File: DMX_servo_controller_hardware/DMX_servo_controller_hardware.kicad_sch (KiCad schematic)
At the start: 6 parts

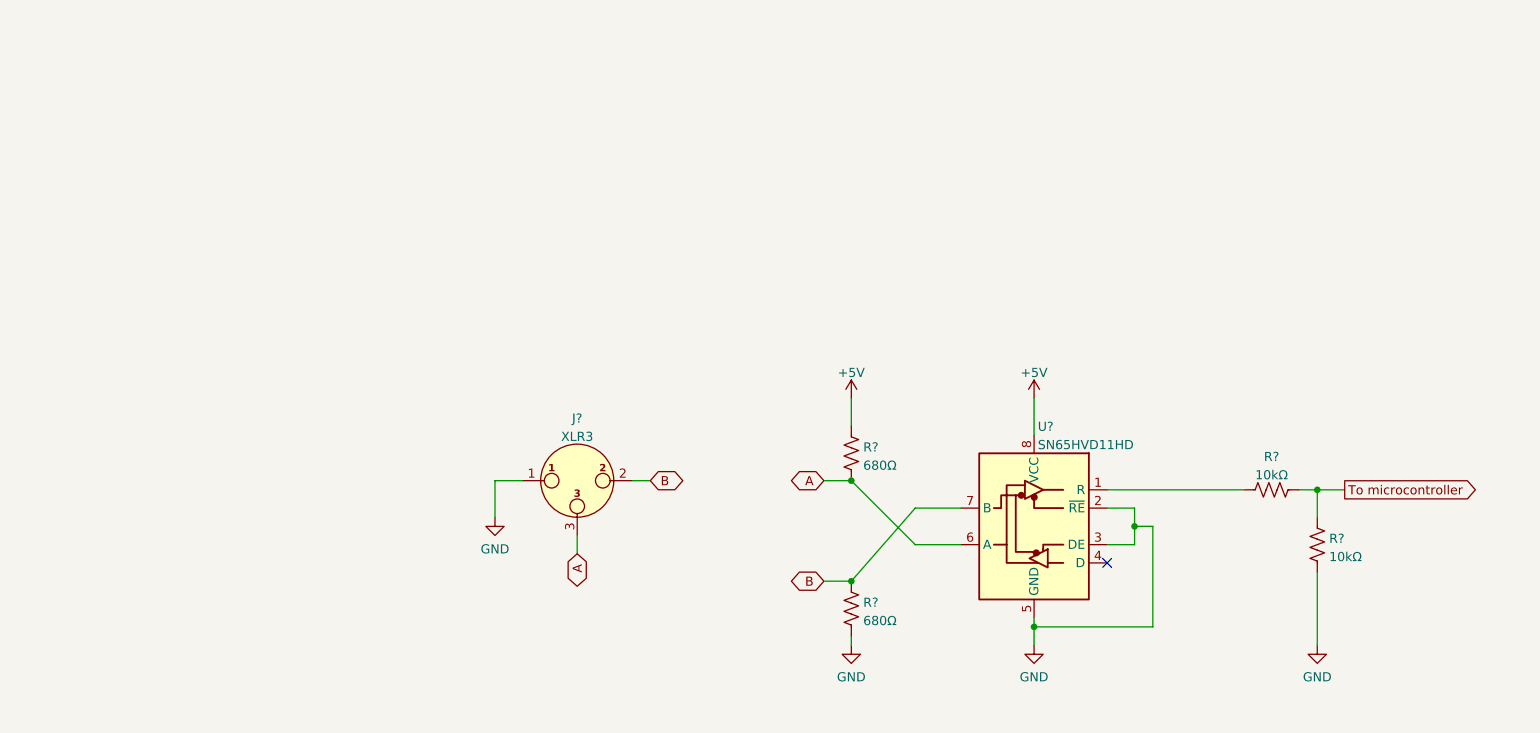
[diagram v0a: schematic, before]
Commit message: Isolates DMX signal from the rest of the electronics
We're using a 0505 5v DC/DC isolator for power and an 6N137 optocoupler
for the signal.

The 6N137 is supposed to work with 5V, but our tests (and other designs)
showed that 3.3V works fine and means the optocoupler works as a level
shifter.
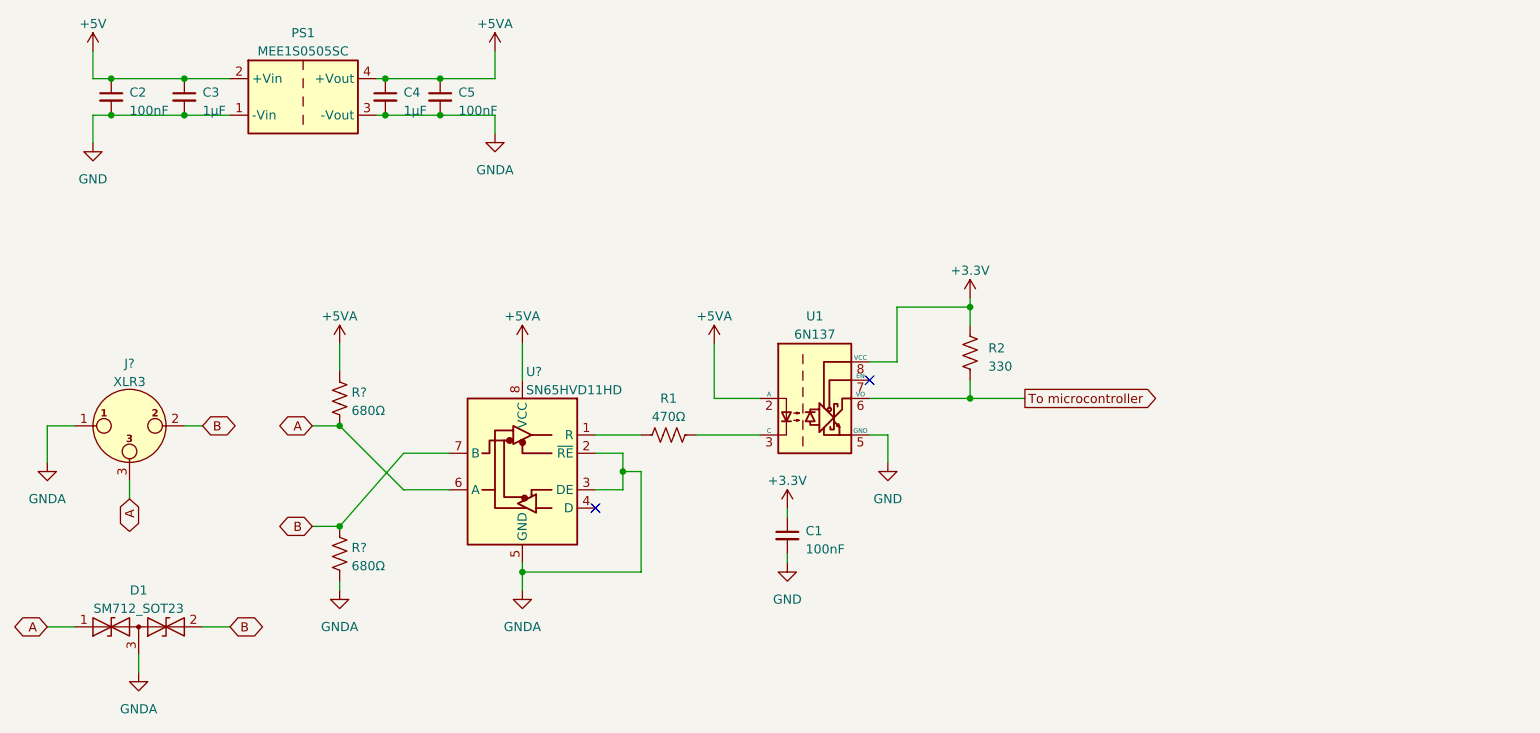
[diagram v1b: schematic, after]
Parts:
- removed R? (x2): 10kΩ, symbol Device:R_US
- added C1, C2, C5: 100nF, symbol Device:C_Small
- added C3, C4: 1μF, symbol Device:C_Small
- added D1: SM712_SOT23, Package_TO_SOT_SMD:SOT-23, symbol Diode:SM712_SOT23
- added PS1: MEE1S0505SC, Converter_DCDC:Converter_DCDC_Murata_MEE1SxxxxSC_THT, symbol Converter_DCDC:MEE1S0505SC
- added R1: 470Ω, symbol Device:R_US
- added R2: 330, symbol Device:R_US
- added U1: 6N137, Package_DIP:DIP-8_W7.62mm, symbol Isolator:6N137
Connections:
- net +5V: now also C2.1, C3.1, PS1.2 (+Vin); no longer R?.1, U?.8 (VCC)
- net A: now also D1.1 (A1)
- net B: now also D1.2 (A2)
- net GND: now also C1.2, C2.2, C3.2, PS1.1 (-Vin), U1.5 (GND); no longer J?.1, R?.2, U?.2 (~{RE}), U?.3 (DE), U?.5 (GND)
- net To microcontroller: now also R2.2, U1.6 (VO)
- net at U?.1 (R): now also R1.2
- new net: R1.1, U1.3 (C)
- new net +3.3V: C1.1, R2.1, U1.8 (VCC)
- new net +5VA: C4.1, C5.1, PS1.4 (+Vout), R?.1, U1.2 (A), U?.8 (VCC)
- new net GNDA: C4.2, C5.2, D1.3 (common), J?.1, PS1.3 (-Vout), R?.2, U?.2 (~{RE}), U?.3 (DE), U?.5 (GND)
- no-connect marks 1 -> 2
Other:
- moved on the sheet: J?, R?, U?

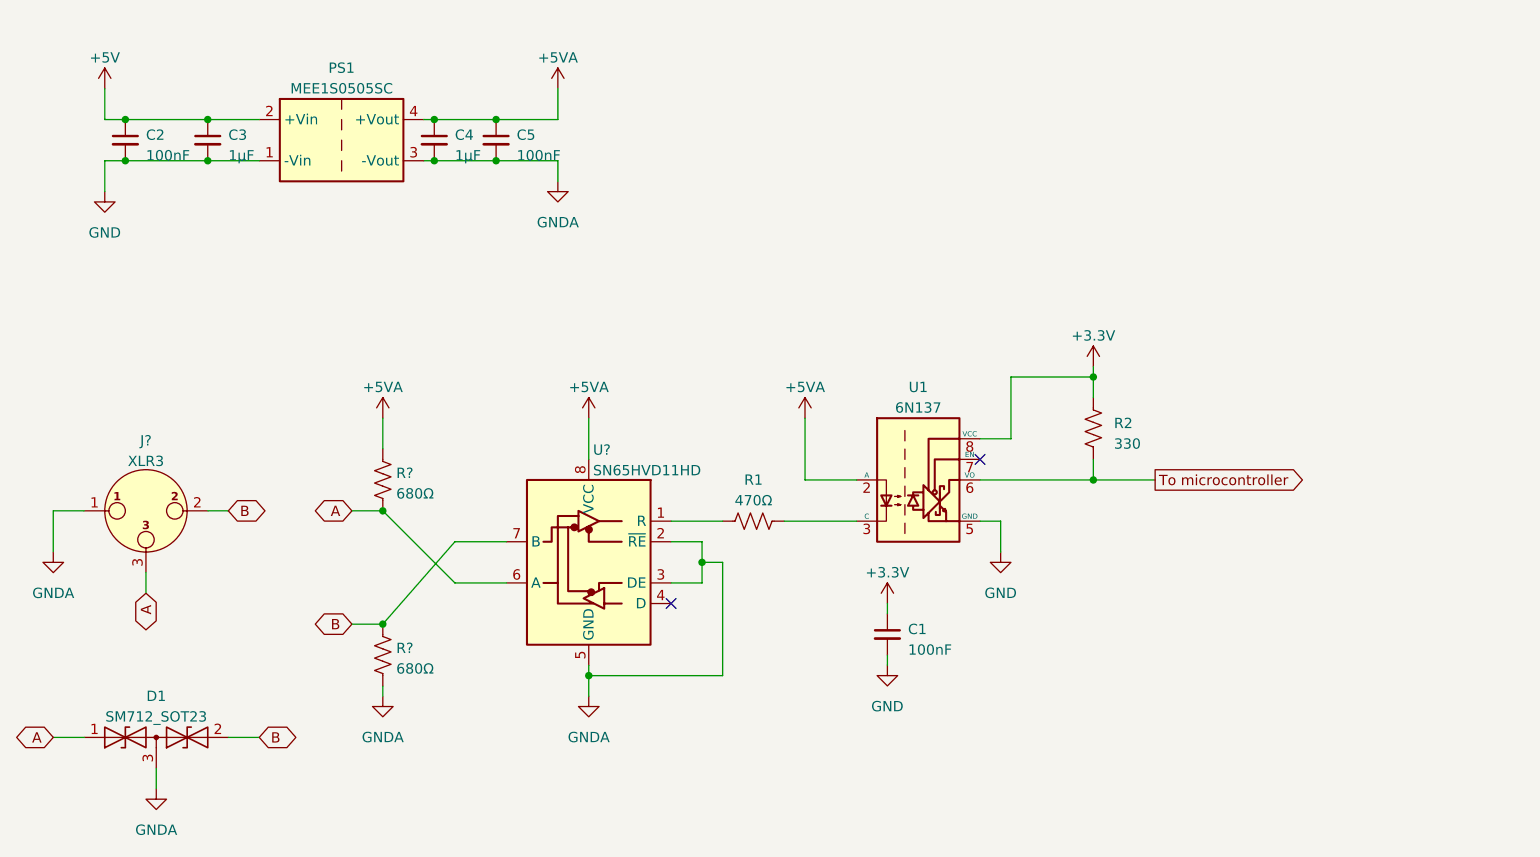
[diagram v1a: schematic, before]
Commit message: Moves XLR connector to a hierarchical sheet
The XLR connectors will be in a daughter board that can be used as a
breakout board for XLR connectors.
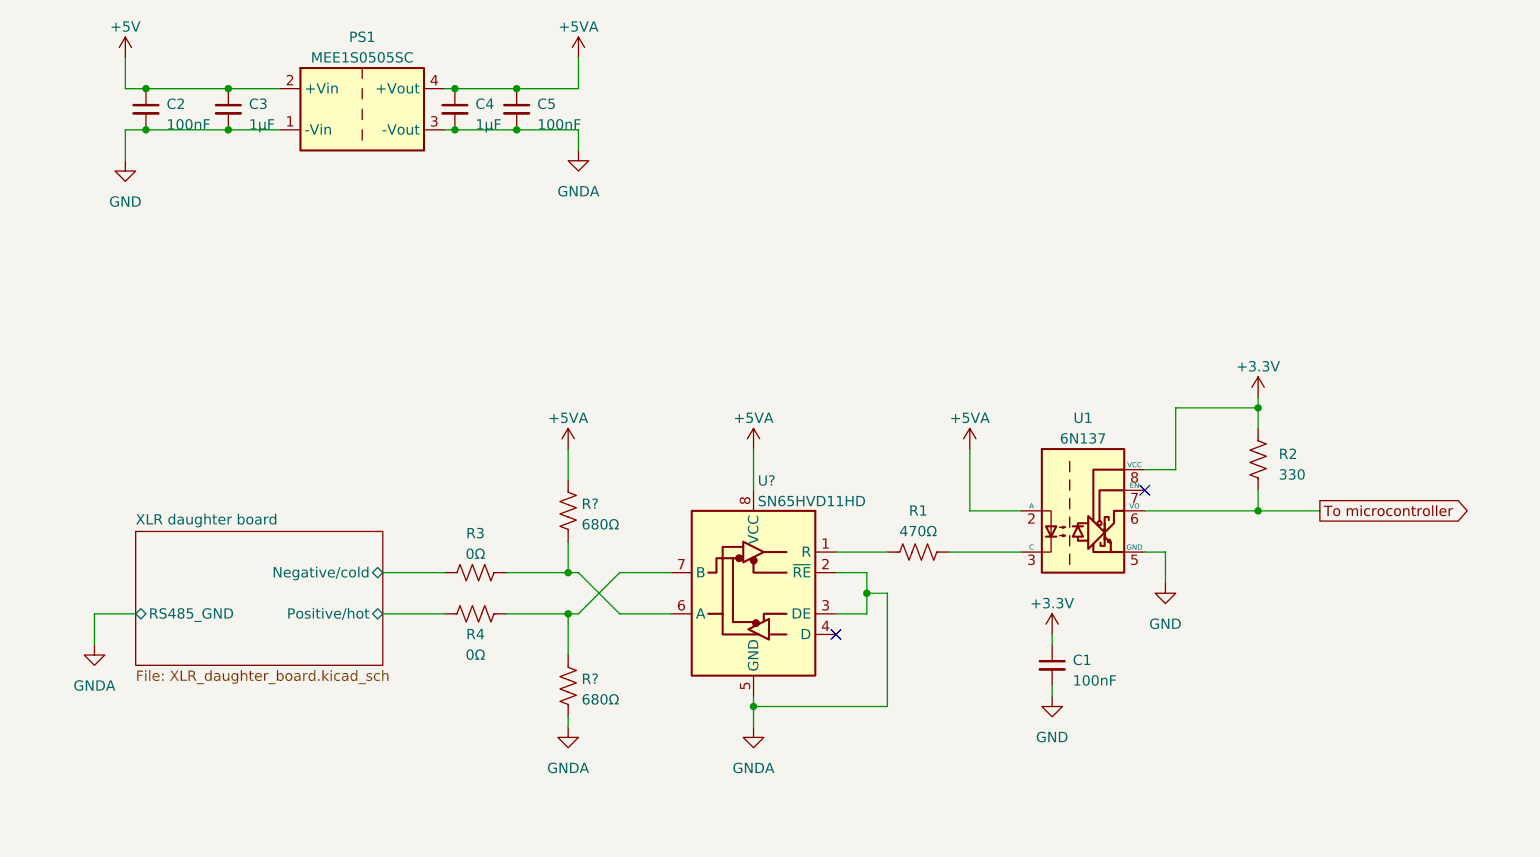
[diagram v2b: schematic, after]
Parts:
- removed D1: SM712_SOT23, Package_TO_SOT_SMD:SOT-23, symbol Diode:SM712_SOT23
- removed J?: XLR3, symbol Connector:XLR3
- added R3, R4: 0Ω, symbol Device:R_US
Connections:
- net A: no longer names the net of R?.2, U?.6 (A)
- net A: now also R3.2
- net B: no longer names the net of R?.1, U?.7 (B)
- net B: now also R4.2
- new net XLR daughter board/Negative/cold: R3.1
- new net XLR daughter board/Positive/hot: R4.1
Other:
- added sheet XLR daughter board (XLR_daughter_board.kicad_sch)
- moved on the sheet: C1, C2, C3, C4, C5, PS1, R1, R2, R?, U1, U?

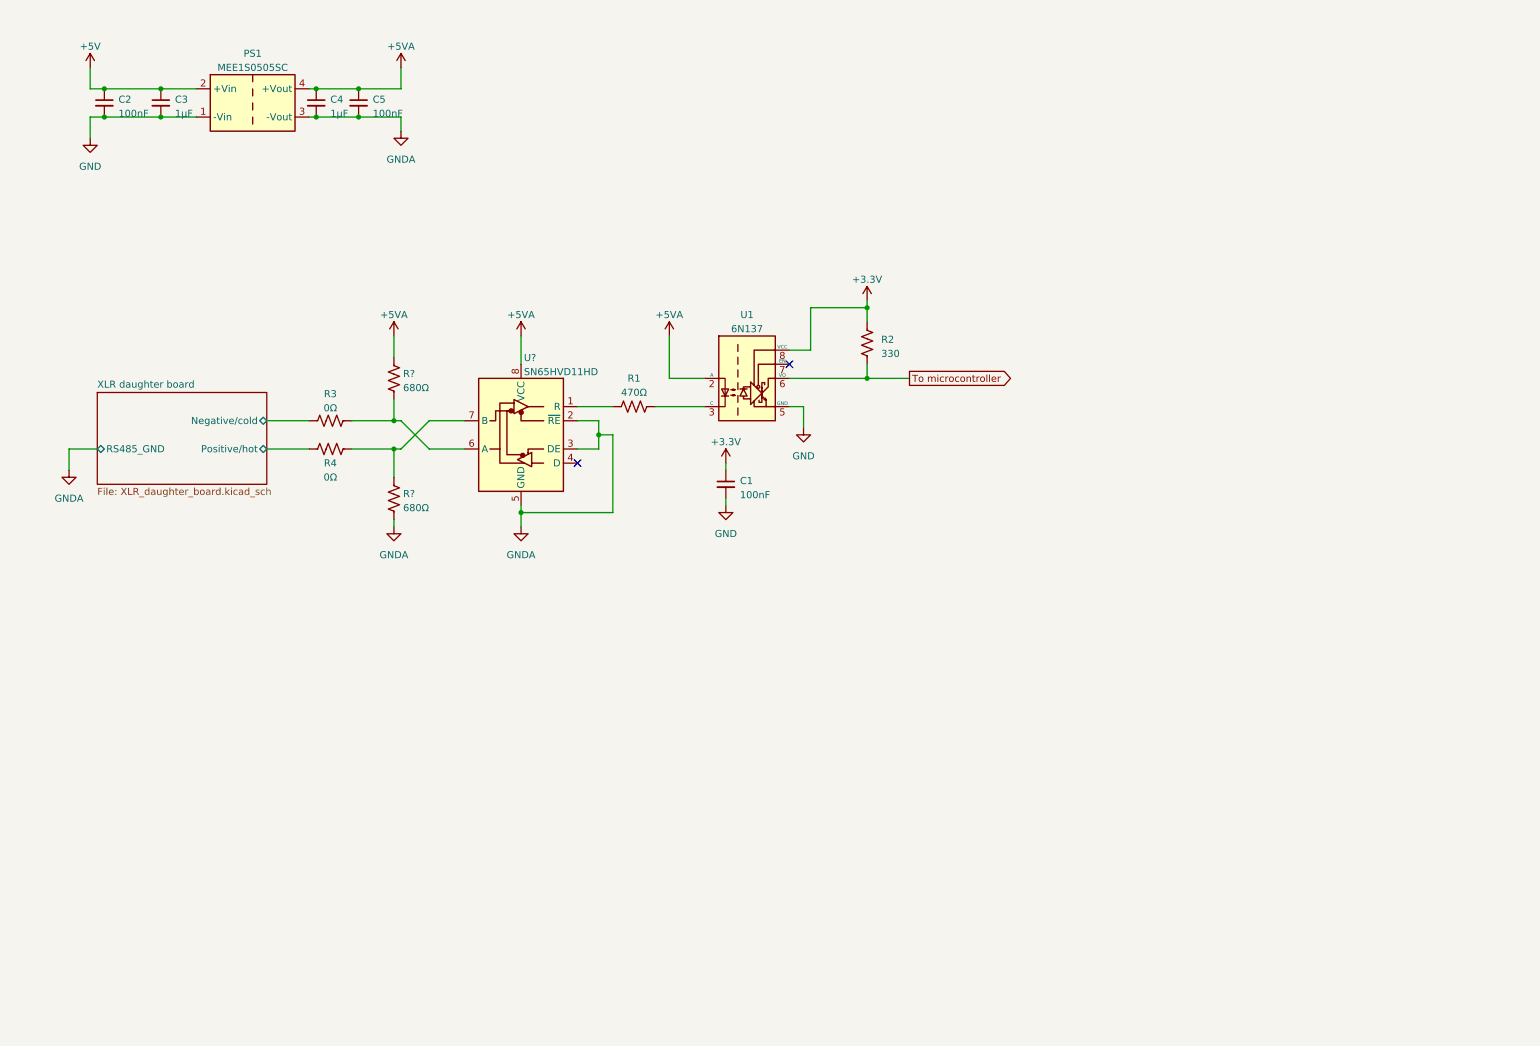
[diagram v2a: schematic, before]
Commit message: Adds Pi Pico to the schematics
This also adds a connector for 5V power (a screw terminal that will be
connected to the external power supply). The 3v3 rail will come from the
pico's regulator.
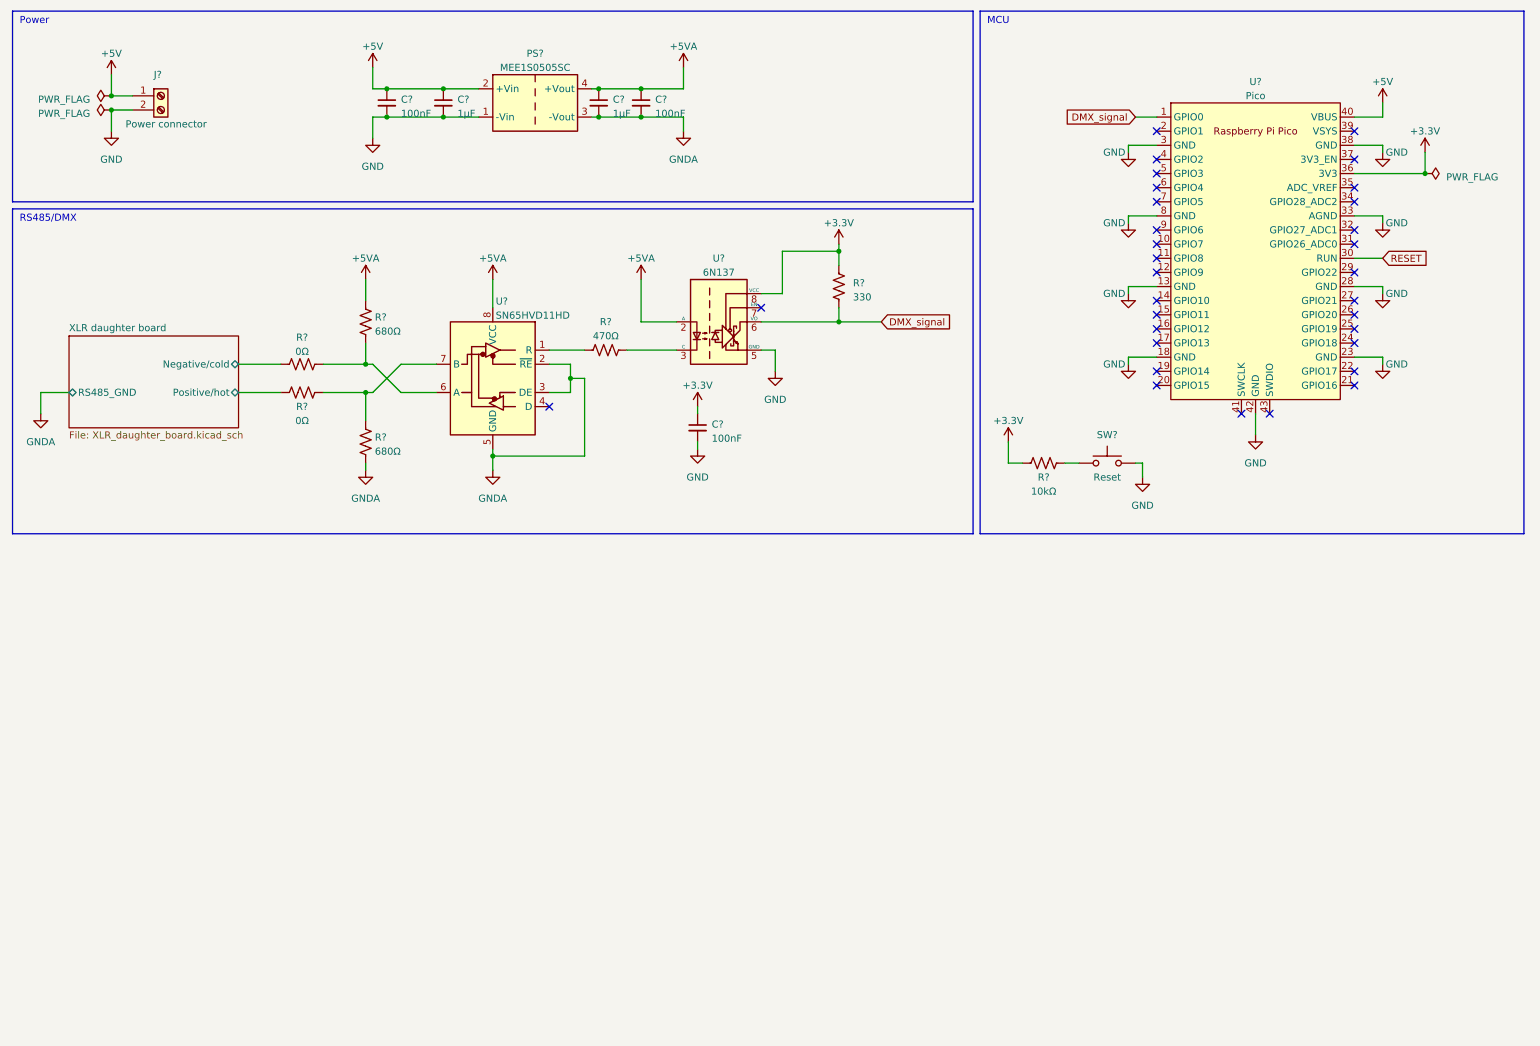
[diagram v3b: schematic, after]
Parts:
- added J?: Power connector, symbol Connector:Screw_Terminal_01x02
- added R?: 10kΩ, symbol Device:R_US
- added SW?: Reset, symbol Switch:SW_Push
- added U?: Pico, RPi_Pico:RPi_Pico_SMD_TH, symbol Pi_Pico:Pico
- renumbered C2 to C?, C3 to C?, C1 to C?, C4 to C?, C5 to C?, PS1 to PS?, R4 to R?, R3 to R?, R2 to R?, R1 to R?, U1 to U?
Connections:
- net +3.3V: now also R?.1, U?.36 (3V3)
- net +5V: now also J?.1 (Pin_1), U?.40 (VBUS)
- net GND: now also J?.2 (Pin_2), SW?.2, U?.13 (GND), U?.18 (GND), U?.23 (GND), U?.28 (GND), U?.3 (GND), U?.33 (AGND), U?.38 (GND), U?.42 (GND), U?.8 (GND)
- net To microcontroller renamed DMX_signal
- net DMX_signal: now also U?.1 (GPIO0)
- new net: R?.2, SW?.1
- new net RESET: U?.30 (RUN)
- no-connect marks 2 -> 32
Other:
- note added: "MCU"
- note added: "Power"
- note added: "RS485/DMX"
- moved on the sheet: C?, PS?, R?, U?
